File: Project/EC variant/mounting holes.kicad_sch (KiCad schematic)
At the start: 20 parts

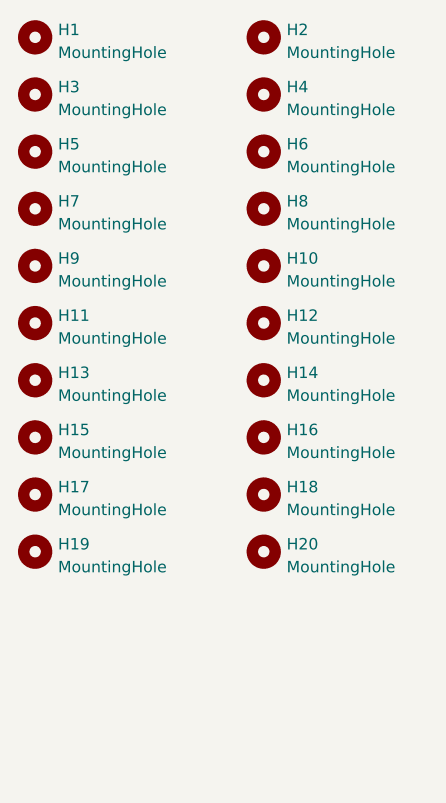
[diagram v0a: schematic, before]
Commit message: changes to topre version and BLE version
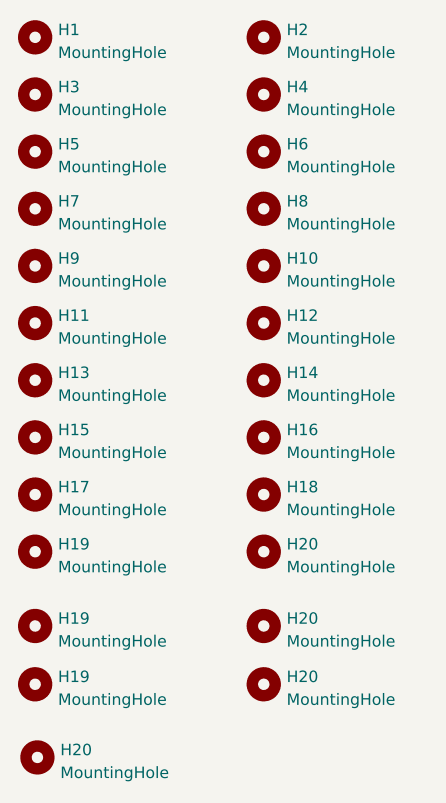
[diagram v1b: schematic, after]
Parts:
- added H19 (x2), H20 (x3): MountingHole, cipulot_parts:HOLE_M2, symbol Mechanical:MountingHole
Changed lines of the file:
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@@
+    )
+  )
+  (symbol (lib_id "Mechanical:MountingHole") (at 63.5 101.092 0) (unit 1)
+    (in_bom yes) (on_board yes) (dnp no) (fields_autoplaced)
+    (property "Reference" "H20" (at 66.04 100.2573 0)
+      (effects (font (size 1.27 1.27)) (justify left))
+    )
+    (property "Value" "MountingHole" (at 66.04 102.7942 0)
+      (effects (font (size 1.27 1.27)) (justify left))
+    )
+    (property "Footprint" "cipulot_parts:HOLE_M2" (at 63.5 101.092 0)
+      (effects (font (size 1.27 1.27)) hide)
+    )
+    (property "Datasheet" "~" (at 63.5 101.092 0)
+      (effects (font (size 1.27 1.27)) hide)
+    )
+    (instances
+      (project "the-nicholas-van"
+        (path "/38f182bd-9097-4ce3-95d4-cd91b210c79b"
+          (reference "H20") (unit 1)
+        )
+        (path "/38f182bd-9097-4ce3-95d4-cd91b210c79b/610cabd0-87c8-472b-8f6a-63e84b5c9031"
+          (reference "H20") (unit 1)
+        )
+      )
+      (project "travaulta"
+        (path "/690df46b-b605-4617-b545-6aaced86d0fc/794114ef-7db2-4f90-86d0-13c32bb11aa3"
+          (reference "H13") (unit 1)
+        )
+      )
+      (project "pandemonium EC 2 Layer"
+        (path "/d73b7c39-1103-4a4e-9b7b-eba7e04e02d3/6fd61ab6-f329-4503-b0b3-34a5cda182cb"
+          (reference "H24") (unit 1)
+        )
+      )
+      (project "EC60"
+        (path "/e63e39d7-6ac0-4ffd-8aa3-1841a4541b55/004107b0-ccf4-476d-9504-97bf1a9256af"
+          (reference "H1") (unit 1)
+        )
+      )
+      (project "forti EC"
+        (path "/f5e5948c-eeca-4160-a5f8-686f765d01ce/55e2d8c6-9092-40f0-965e-73dea8a35aef"
+          (reference "H20") (unit 1)
+        )
+      )
+    )
+  )
+  (symbol (lib_id "Mechanical:MountingHole") (at 38.354 109.22 0) (unit 1)
+    (in_bom yes) (on_board yes) (dnp no) (fields_autoplaced)
+    (property "Reference" "H20" (at 40.894 108.3853 0)
+      (effects (font (size 1.27 1.27)) (justify left))
+    )
+    (property "Value" "MountingHole" (at 40.894 110.9222 0)
+      (effects (font (size 1.27 1.27)) (justify left))
+    )
+    (property "Footprint" "cipulot_parts:HOLE_M2" (at 38.354 109.22 0)
+      (effects (font (size 1.27 1.27)) hide)
+    )
+    (property "Datasheet" "~" (at 38.354 109.22 0)
+      (effects (font (size 1.27 1.27)) hide)
+    )
+    (instances
+      (project "the-nicholas-van"
+        (path "/38f182bd-9097-4ce3-95d4-cd91b210c79b"
+          (reference "H20") (unit 1)
+        )
+        (path "/38f182bd-9097-4ce3-95d4-cd91b210c79b/610cabd0-87c8-472b-8f6a-63e84b5c9031"
+          (reference "H20") (unit 1)
+        )
+      )
+      (project "travaulta"
+        (path "/690df46b-b605-4617-b545-6aaced86d0fc/794114ef-7db2-4f90-86d0-13c32bb11aa3"
+          (reference "H13") (unit 1)
+        )
+      )
+      (project "pandemonium EC 2 Layer"
+        (path "/d73b7c39-1103-4a4e-9b7b-eba7e04e02d3/6fd61ab6-f329-4503-b0b3-34a5cda182cb"
+          (reference "H25") (unit 1)
+        )
+      )
+      (project "EC60"
+        (path "/e63e39d7-6ac0-4ffd-8aa3-1841a4541b55/004107b0-ccf4-476d-9504-97bf1a9256af"
+          (reference "H1") (unit 1)
+        )
+      )
+      (project "forti EC"
+        (path "/f5e5948c-eeca-4160-a5f8-686f765d01ce/55e2d8c6-9092-40f0-965e-73dea8a35aef"
+          (reference "H20") (unit 1)
+        )
+      )
     )
   )
@@
     )
   )
+  (symbol (lib_id "Mechanical:MountingHole") (at 38.1 101.092 0) (unit 1)
+    (in_bom yes) (on_board yes) (dnp no) (fields_autoplaced)
+    (property "Reference" "H19" (at 40.64 100.2573 0)
+      (effects (font (size 1.27 1.27)) (justify left))
+    )
+    (property "Value" "MountingHole" (at 40.64 102.7942 0)
+      (effects (font (size 1.27 1.27)) (justify left))
+    )
+    (property "Footprint" "cipulot_parts:HOLE_M2" (at 38.1 101.092 0)
+      (effects (font (size 1.27 1.27)) hide)
+    )
+    (property "Datasheet" "~" (at 38.1 101.092 0)
+      (effects (font (size 1.27 1.27)) hide)
+    )
+    (instances
+      (project "the-nicholas-van"
+        (path "/38f182bd-9097-4ce3-95d4-cd91b210c79b"
+          (reference "H19") (unit 1)
+        )
+        (path "/38f182bd-9097-4ce3-95d4-cd91b210c79b/610cabd0-87c8-472b-8f6a-63e84b5c9031"
+          (reference "H19") (unit 1)
+        )
+      )
+      (project "travaulta"
+        (path "/690df46b-b605-4617-b545-6aaced86d0fc/794114ef-7db2-4f90-86d0-13c32bb11aa3"
+          (reference "H5") (unit 1)
+        )
+      )
+      (project "pandemonium EC 2 Layer"
+        (path "/d73b7c39-1103-4a4e-9b7b-eba7e04e02d3/6fd61ab6-f329-4503-b0b3-34a5cda182cb"
+          (reference "H23") (unit 1)
+        )
+      )
+      (project "EC60"
+        (path "/e63e39d7-6ac0-4ffd-8aa3-1841a4541b55/004107b0-ccf4-476d-9504-97bf1a9256af"
+          (reference "H1") (unit 1)
+        )
+      )
+      (project "forti EC"
+        (path "/f5e5948c-eeca-4160-a5f8-686f765d01ce/55e2d8c6-9092-40f0-965e-73dea8a35aef"
+          (reference "H19") (unit 1)
+        )
+      )
+    )
+  )
   (symbol (lib_id "Mechanical:MountingHole") (at 63.5 48.26 0) (unit 1)
     (in_bom yes) (on_board yes) (dnp no) (fields_autoplaced)
@@
     )
   )
+  (symbol (lib_id "Mechanical:MountingHole") (at 38.1 94.615 0) (unit 1)
+    (in_bom yes) (on_board yes) (dnp no) (fields_autoplaced)
+    (property "Reference" "H19" (at 40.64 93.7803 0)
+      (effects (font (size 1.27 1.27)) (justify left))
+    )
+    (property "Value" "MountingHole" (at 40.64 96.3172 0)
+      (effects (font (size 1.27 1.27)) (justify left))
+    )
+    (property "Footprint" "cipulot_parts:HOLE_M2" (at 38.1 94.615 0)
+      (effects (font (size 1.27 1.27)) hide)
+    )
+    (property "Datasheet" "~" (at 38.1 94.615 0)
+      (effects (font (size 1.27 1.27)) hide)
+    )
+    (instances
+      (project "the-nicholas-van"
+        (path "/38f182bd-9097-4ce3-95d4-cd91b210c79b"
+          (reference "H19") (unit 1)
+        )
+        (path "/38f182bd-9097-4ce3-95d4-cd91b210c79b/610cabd0-87c8-472b-8f6a-63e84b5c9031"
+          (reference "H19") (unit 1)
+        )
+      )
+      (project "travaulta"
+        (path "/690df46b-b605-4617-b545-6aaced86d0fc/794114ef-7db2-4f90-86d0-13c32bb11aa3"
+          (reference "H5") (unit 1)
+        )
+      )
+      (project "pandemonium EC 2 Layer"
+        (path "/d73b7c39-1103-4a4e-9b7b-eba7e04e02d3/6fd61ab6-f329-4503-b0b3-34a5cda182cb"
+          (reference "H21") (unit 1)
+        )
+      )
+      (project "EC60"
+        (path "/e63e39d7-6ac0-4ffd-8aa3-1841a4541b55/004107b0-ccf4-476d-9504-97bf1a9256af"
+          (reference "H1") (unit 1)
+        )
+      )
+      (project "forti EC"
+        (path "/f5e5948c-eeca-4160-a5f8-686f765d01ce/55e2d8c6-9092-40f0-965e-73dea8a35aef"
+          (reference "H19") (unit 1)
+        )
+      )
+    )
+  )
   (symbol (lib_id "Mechanical:MountingHole") (at 38.1 48.26 0) (unit 1)
     (in_bom yes) (on_board yes) (dnp no) (fields_autoplaced)
@@
         )
       )
+    )
+  )
+  (symbol (lib_id "Mechanical:MountingHole") (at 63.5 94.615 0) (unit 1)
+    (in_bom yes) (on_board yes) (dnp no) (fields_autoplaced)
+    (property "Reference" "H20" (at 66.04 93.7803 0)
+      (effects (font (size 1.27 1.27)) (justify left))
+    )
+    (property "Value" "MountingHole" (at 66.04 96.3172 0)
+      (effects (font (size 1.27 1.27)) (justify left))
+    )
+    (property "Footprint" "cipulot_parts:HOLE_M2" (at 63.5 94.615 0)
+      (effects (font (size 1.27 1.27)) hide)
+    )
+    (property "Datasheet" "~" (at 63.5 94.615 0)
+      (effects (font (size 1.27 1.27)) hide)
+    )
+    (instances
+      (project "the-nicholas-van"
+        (path "/38f182bd-9097-4ce3-95d4-cd91b210c79b"
+          (reference "H20") (unit 1)
+        )
+        (path "/38f182bd-9097-4ce3-95d4-cd91b210c79b/610cabd0-87c8-472b-8f6a-63e84b5c9031"
+          (reference "H20") (unit 1)
+        )
+      )
+      (project "travaulta"
+        (path "/690df46b-b605-4617-b545-6aaced86d0fc/794114ef-7db2-4f90-86d0-13c32bb11aa3"
+          (reference "H13") (unit 1)
+        )
+      )
+      (project "pandemonium EC 2 Layer"
+        (path "/d73b7c39-1103-4a4e-9b7b-eba7e04e02d3/6fd61ab6-f329-4503-b0b3-34a5cda182cb"
+          (reference "H22") (unit 1)
+        )
+      )
+      (project "EC60"
+        (path "/e63e39d7-6ac0-4ffd-8aa3-1841a4541b55/004107b0-ccf4-476d-9504-97bf1a9256af"
+          (reference "H1") (unit 1)
+        )
+      )
+      (project "forti EC"
+        (path "/f5e5948c-eeca-4160-a5f8-686f765d01ce/55e2d8c6-9092-40f0-965e-73dea8a35aef"
+          (reference "H20") (unit 1)
+        )
+      )
